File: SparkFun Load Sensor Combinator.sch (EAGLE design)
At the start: 12 parts

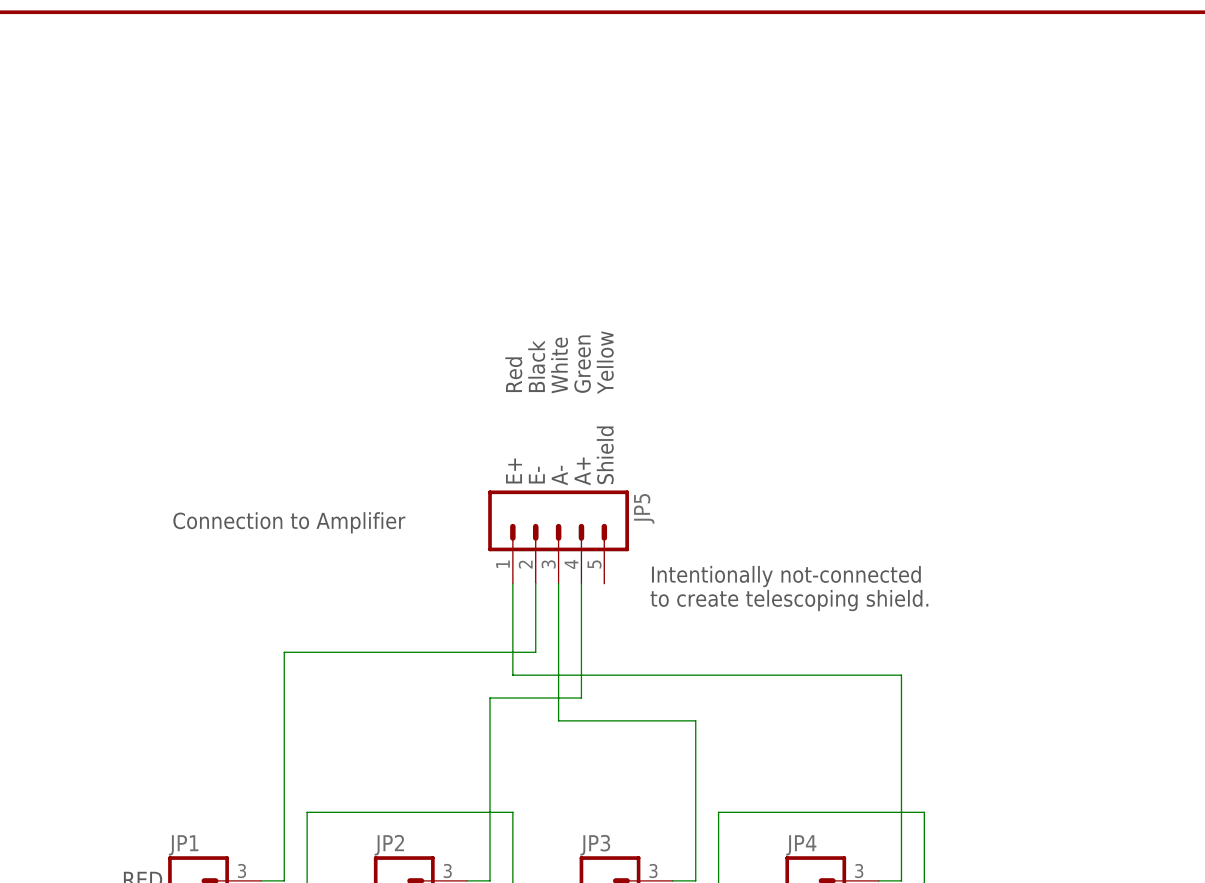
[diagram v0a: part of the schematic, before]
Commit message: Added RJ45
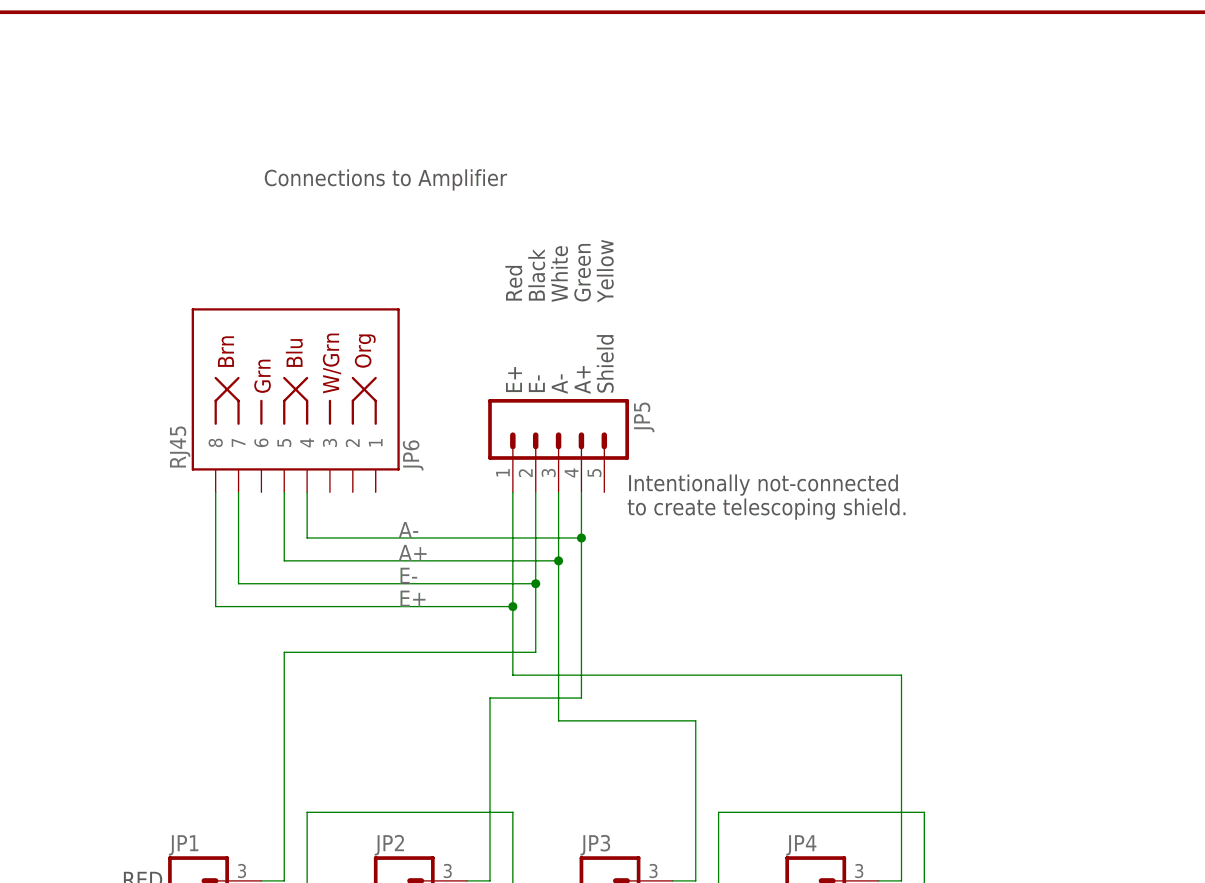
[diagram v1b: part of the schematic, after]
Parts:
- added JP6: RJ45, SparkFun-Connectors:RJ45-8PTH
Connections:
- net A+: now also JP6.5
- net A-: now also JP6.4
- net E+: now also JP6.8
- net E-: now also JP6.7
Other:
- note added: "Connections to Amplifier"
- note removed: "Connection to Amplifier"
- moved on the sheet: JP5
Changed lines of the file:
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@@
 <?xml version="1.0" encoding="utf-8"?>
 <!DOCTYPE eagle SYSTEM "eagle.dtd">
-<eagle version="7.2.0">
+<eagle version="7.1.0">
 <drawing>
 <settings>
@@
 </part>
 <part name="JP5" library="SparkFun-Connectors" deviceset="M05" device="PTH"/>
+<part name="JP6" library="SparkFun-Connectors" deviceset="RJ45-8" device="PTH" value="RJ45"/>
 </parts>
 <sheets>
 <sheet>
 <plain>
-<text x="120.396" y="132.842" size="1.778" layer="97" rot="R90">E+</text>
-<text x="122.936" y="132.842" size="1.778" layer="97" rot="R90">E-</text>
-<text x="125.476" y="132.842" size="1.778" layer="97" rot="R90">A-</text>
-<text x="128.016" y="132.842" size="1.778" layer="97" rot="R90">A+</text>
-<text x="120.396" y="143.002" size="1.778" layer="97" rot="R90">Red</text>
-<text x="122.936" y="143.002" size="1.778" layer="97" rot="R90">Black</text>
-<text x="125.476" y="143.002" size="1.778" layer="97" rot="R90">White</text>
-<text x="128.016" y="143.002" size="1.778" layer="97" rot="R90">Green</text>
+<text x="120.396" y="143.002" size="1.778" layer="97" rot="R90">E+</text>
+<text x="122.936" y="143.002" size="1.778" layer="97" rot="R90">E-</text>
+<text x="125.476" y="143.002" size="1.778" layer="97" rot="R90">A-</text>
+<text x="128.016" y="143.002" size="1.778" layer="97" rot="R90">A+</text>
+<text x="120.396" y="153.162" size="1.778" layer="97" rot="R90">Red</text>
+<text x="122.936" y="153.162" size="1.778" layer="97" rot="R90">Black</text>
+<text x="125.476" y="153.162" size="1.778" layer="97" rot="R90">White</text>
+<text x="128.016" y="153.162" size="1.778" layer="97" rot="R90">Green</text>
 <text x="147.32" y="68.58" size="1.778" layer="97">Lower Right</text>
 <text x="101.6" y="68.58" size="1.778" layer="97">Upper Right</text>
@@
 <text x="106.68" y="60.96" size="1.778" layer="97">3-Wire Load Sensors</text>
 <text x="105.41" y="63.754" size="1.778" layer="97">Common Bathroom Scale</text>
-<text x="81.534" y="128.016" size="1.778" layer="97">Connection to Amplifier</text>
+<text x="91.694" y="166.116" size="1.778" layer="97">Connections to Amplifier</text>
 <text x="75.692" y="82.804" size="1.778" layer="97">BLK</text>
 <text x="75.946" y="85.598" size="1.778" layer="97">WHT</text>
 <text x="75.946" y="88.138" size="1.778" layer="97">RED</text>
 <text x="83.82" y="53.34" size="2.032" layer="97">4 load sensors combine to create one load cell</text>
-<text x="130.556" y="132.842" size="1.778" layer="97" rot="R90">Shield</text>
-<text x="130.556" y="143.002" size="1.778" layer="97" rot="R90">Yellow</text>
-<text x="134.62" y="119.38" size="1.778" layer="97">Intentionally not-connected
+<text x="130.556" y="143.002" size="1.778" layer="97" rot="R90">Shield</text>
+<text x="130.556" y="153.162" size="1.778" layer="97" rot="R90">Yellow</text>
+<text x="132.08" y="129.54" size="1.778" layer="97">Intentionally not-connected
 to create telescoping shield.</text>
 </plain>
@@
 </instance>
 <instance part="FRAME1" gate="V" x="147.32" y="0"/>
-<instance part="JP5" gate="G$1" x="124.46" y="129.54" rot="R270"/>
+<instance part="JP5" gate="G$1" x="124.46" y="139.7" rot="R270"/>
+<instance part="JP6" gate="JP1" x="96.52" y="139.7" rot="MR90"/>
 </instances>
 <busses>
@@
 <wire x1="162.56" y1="88.9" x2="162.56" y2="111.76" width="0.1524" layer="91"/>
 <wire x1="119.38" y1="111.76" x2="162.56" y2="111.76" width="0.1524" layer="91"/>
-<wire x1="119.38" y1="111.76" x2="119.38" y2="121.92" width="0.1524" layer="91"/>
+<wire x1="119.38" y1="111.76" x2="119.38" y2="119.38" width="0.1524" layer="91"/>
 <pinref part="JP5" gate="G$1" pin="1"/>
+<wire x1="119.38" y1="119.38" x2="119.38" y2="132.08" width="0.1524" layer="91"/>
+<wire x1="119.38" y1="119.38" x2="86.36" y2="119.38" width="0.1524" layer="91"/>
+<wire x1="86.36" y1="119.38" x2="86.36" y2="132.08" width="0.1524" layer="91"/>
+<junction x="119.38" y="119.38"/>
+<pinref part="JP6" gate="JP1" pin="8"/>
+<label x="106.68" y="119.38" size="1.778" layer="95"/>
 </segment>
 </net>
@@
 <pinref part="JP3" gate="G$1" pin="3"/>
 <wire x1="139.7" y1="88.9" x2="137.16" y2="88.9" width="0.1524" layer="91"/>
-<wire x1="124.46" y1="106.68" x2="124.46" y2="121.92" width="0.1524" layer="91"/>
+<wire x1="124.46" y1="106.68" x2="124.46" y2="124.46" width="0.1524" layer="91"/>
 <pinref part="JP5" gate="G$1" pin="3"/>
+<wire x1="124.46" y1="124.46" x2="124.46" y2="132.08" width="0.1524" layer="91"/>
+<wire x1="124.46" y1="124.46" x2="93.98" y2="124.46" width="0.1524" layer="91"/>
+<junction x="124.46" y="124.46"/>
+<pinref part="JP6" gate="JP1" pin="5"/>
+<wire x1="93.98" y1="132.08" x2="93.98" y2="124.46" width="0.1524" layer="91"/>
+<label x="106.68" y="124.46" size="1.778" layer="95"/>
 </segment>
 </net>
@@
 <wire x1="116.84" y1="88.9" x2="116.84" y2="109.22" width="0.1524" layer="91"/>
 <wire x1="116.84" y1="109.22" x2="127" y2="109.22" width="0.1524" layer="91"/>
-<wire x1="127" y1="121.92" x2="127" y2="109.22" width="0.1524" layer="91"/>
+<wire x1="127" y1="132.08" x2="127" y2="127" width="0.1524" layer="91"/>
 <pinref part="JP5" gate="G$1" pin="4"/>
+<wire x1="127" y1="127" x2="127" y2="109.22" width="0.1524" layer="91"/>
+<wire x1="127" y1="127" x2="96.52" y2="127" width="0.1524" layer="91"/>
+<junction x="127" y="127"/>
+<pinref part="JP6" gate="JP1" pin="4"/>
+<wire x1="96.52" y1="132.08" x2="96.52" y2="127" width="0.1524" layer="91"/>
+<label x="106.68" y="127" size="1.778" layer="95"/>
 </segment>
 </net>
@@
 <segment>
 <wire x1="121.92" y1="114.3" x2="121.92" y2="121.92" width="0.1524" layer="91"/>
+<wire x1="121.92" y1="121.92" x2="121.92" y2="132.08" width="0.1524" layer="91"/>
 <wire x1="121.92" y1="114.3" x2="93.98" y2="114.3" width="0.1524" layer="91"/>
 <wire x1="93.98" y1="114.3" x2="93.98" y2="88.9" width="0.1524" layer="91"/>
@@
 <wire x1="93.98" y1="88.9" x2="91.44" y2="88.9" width="0.1524" layer="91"/>
 <pinref part="JP5" gate="G$1" pin="2"/>
-</segment>
-</net>
+<wire x1="121.92" y1="121.92" x2="88.9" y2="121.92" width="0.1524" layer="91"/>
+<wire x1="88.9" y1="121.92" x2="88.9" y2="132.08" width="0.1524" layer="91"/>
+<junction x="121.92" y="121.92"/>
+<pinref part="JP6" gate="JP1" pin="7"/>
+<label x="106.68" y="121.92" size="1.778" layer="95"/>
+</segment>
+</net>

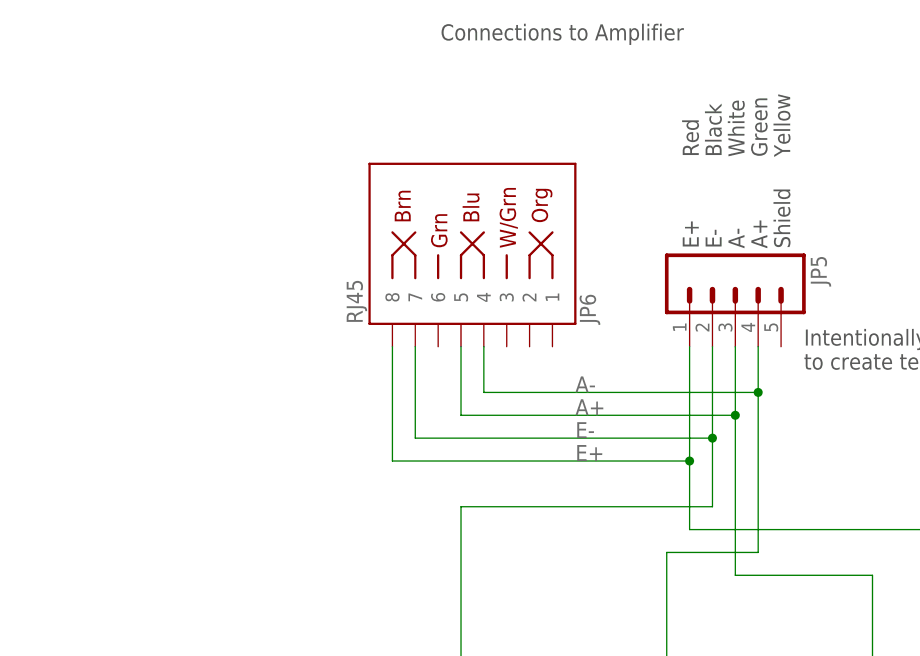
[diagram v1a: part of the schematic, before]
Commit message: Added DS18S20 connection.
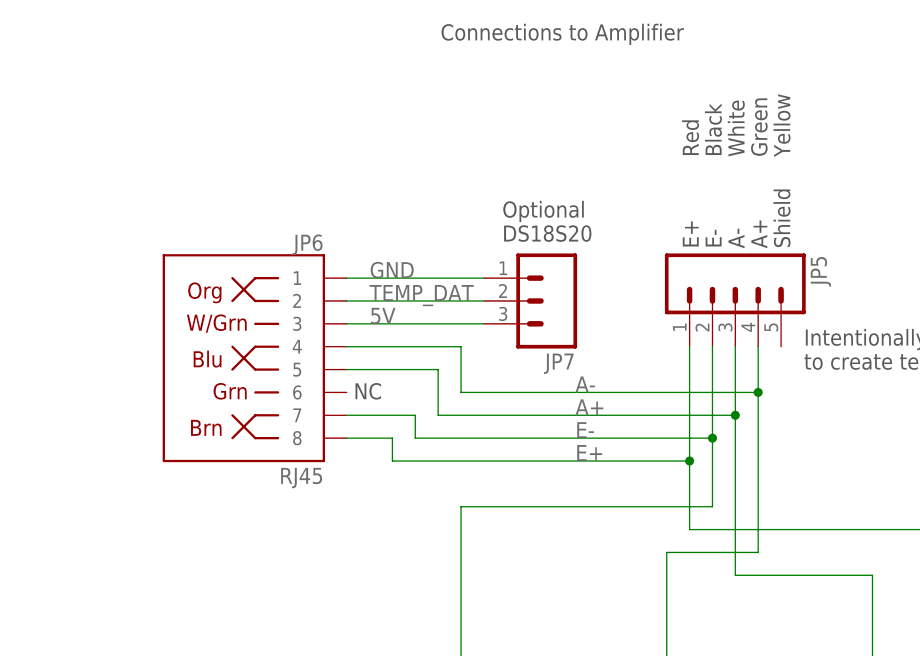
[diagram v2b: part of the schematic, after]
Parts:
- added JP7: (no value), SparkFun-Connectors:M03PTH
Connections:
- new net 5V: JP6.3, JP7.3
- new net GND: JP6.1, JP7.1
- new net TEMP_DAT: JP6.2, JP7.2
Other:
- note added: "NC"
- note added: "Optional DS18S20"
- moved on the sheet: JP6
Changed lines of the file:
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@@
 <part name="JP5" library="SparkFun-Connectors" deviceset="M05" device="PTH"/>
 <part name="JP6" library="SparkFun-Connectors" deviceset="RJ45-8" device="PTH" value="RJ45"/>
+<part name="JP7" library="SparkFun-Connectors" deviceset="M03" device="PTH"/>
 </parts>
 <sheets>
@@
 <text x="132.08" y="129.54" size="1.778" layer="97">Intentionally not-connected
 to create telescoping shield.</text>
+<text x="82.042" y="126.238" size="1.778" layer="97">NC</text>
+<text x="98.552" y="143.764" size="1.778" layer="97">Optional
+DS18S20</text>
 </plain>
 <instances>
@@
 <instance part="FRAME1" gate="V" x="147.32" y="0"/>
 <instance part="JP5" gate="G$1" x="124.46" y="139.7" rot="R270"/>
-<instance part="JP6" gate="JP1" x="96.52" y="139.7" rot="MR90"/>
+<instance part="JP6" gate="JP1" x="73.66" y="132.08" rot="MR0"/>
+<instance part="JP7" gate="G$1" x="104.14" y="137.16" rot="R180"/>
 </instances>
 <busses>
@@
 <pinref part="JP5" gate="G$1" pin="1"/>
 <wire x1="119.38" y1="119.38" x2="119.38" y2="132.08" width="0.1524" layer="91"/>
-<wire x1="119.38" y1="119.38" x2="86.36" y2="119.38" width="0.1524" layer="91"/>
-<wire x1="86.36" y1="119.38" x2="86.36" y2="132.08" width="0.1524" layer="91"/>
 <junction x="119.38" y="119.38"/>
 <pinref part="JP6" gate="JP1" pin="8"/>
 <label x="106.68" y="119.38" size="1.778" layer="95"/>
+<wire x1="119.38" y1="119.38" x2="86.36" y2="119.38" width="0.1524" layer="91"/>
+<wire x1="86.36" y1="119.38" x2="86.36" y2="121.92" width="0.1524" layer="91"/>
+<wire x1="86.36" y1="121.92" x2="81.28" y2="121.92" width="0.1524" layer="91"/>
 </segment>
 </net>
@@
 <pinref part="JP5" gate="G$1" pin="3"/>
 <wire x1="124.46" y1="124.46" x2="124.46" y2="132.08" width="0.1524" layer="91"/>
-<wire x1="124.46" y1="124.46" x2="93.98" y2="124.46" width="0.1524" layer="91"/>
+<wire x1="124.46" y1="124.46" x2="91.44" y2="124.46" width="0.1524" layer="91"/>
 <junction x="124.46" y="124.46"/>
 <pinref part="JP6" gate="JP1" pin="5"/>
-<wire x1="93.98" y1="132.08" x2="93.98" y2="124.46" width="0.1524" layer="91"/>
 <label x="106.68" y="124.46" size="1.778" layer="95"/>
+<wire x1="81.28" y1="129.54" x2="91.44" y2="129.54" width="0.1524" layer="91"/>
+<wire x1="91.44" y1="129.54" x2="91.44" y2="124.46" width="0.1524" layer="91"/>
 </segment>
 </net>
@@
 <pinref part="JP5" gate="G$1" pin="4"/>
 <wire x1="127" y1="127" x2="127" y2="109.22" width="0.1524" layer="91"/>
-<wire x1="127" y1="127" x2="96.52" y2="127" width="0.1524" layer="91"/>
+<wire x1="127" y1="127" x2="93.98" y2="127" width="0.1524" layer="91"/>
 <junction x="127" y="127"/>
 <pinref part="JP6" gate="JP1" pin="4"/>
-<wire x1="96.52" y1="132.08" x2="96.52" y2="127" width="0.1524" layer="91"/>
 <label x="106.68" y="127" size="1.778" layer="95"/>
+<wire x1="81.28" y1="132.08" x2="93.98" y2="132.08" width="0.1524" layer="91"/>
+<wire x1="93.98" y1="132.08" x2="93.98" y2="127" width="0.1524" layer="91"/>
 </segment>
 </net>
@@
 <wire x1="93.98" y1="88.9" x2="91.44" y2="88.9" width="0.1524" layer="91"/>
 <pinref part="JP5" gate="G$1" pin="2"/>
-<wire x1="121.92" y1="121.92" x2="88.9" y2="121.92" width="0.1524" layer="91"/>
-<wire x1="88.9" y1="121.92" x2="88.9" y2="132.08" width="0.1524" layer="91"/>
 <junction x="121.92" y="121.92"/>
 <pinref part="JP6" gate="JP1" pin="7"/>
 <label x="106.68" y="121.92" size="1.778" layer="95"/>
+<wire x1="121.92" y1="121.92" x2="88.9" y2="121.92" width="0.1524" layer="91"/>
+<wire x1="88.9" y1="121.92" x2="88.9" y2="124.46" width="0.1524" layer="91"/>
+<wire x1="88.9" y1="124.46" x2="81.28" y2="124.46" width="0.1524" layer="91"/>
 </segment>
 </net>
+<net name="5V" class="0">
+<segment>
+<pinref part="JP6" gate="JP1" pin="3"/>
+<pinref part="JP7" gate="G$1" pin="3"/>
+<wire x1="81.28" y1="134.62" x2="96.52" y2="134.62" width="0.1524" layer="91"/>
+<label x="83.82" y="134.62" size="1.778" layer="95"/>
+</segment>
+</net>
+<net name="TEMP_DAT" class="0">
+<segment>
+<pinref part="JP6" gate="JP1" pin="2"/>
+<pinref part="JP7" gate="G$1" pin="2"/>
+<wire x1="81.28" y1="137.16" x2="96.52" y2="137.16" width="0.1524" layer="91"/>
+<label x="83.82" y="137.16" size="1.778" layer="95"/>
+</segment>
+</net>
+<net name="GND" class="0">
+<segment>
+<pinref part="JP6" gate="JP1" pin="1"/>
+<pinref part="JP7" gate="G$1" pin="1"/>
+<wire x1="81.28" y1="139.7" x2="96.52" y2="139.7" width="0.1524" layer="91"/>
+<label x="83.82" y="139.7" size="1.778" layer="95"/>
+</segment>
+</net>

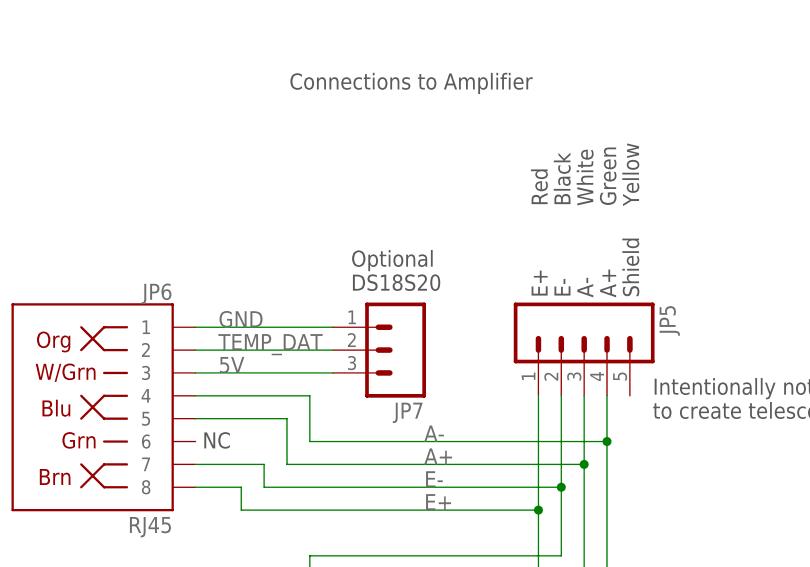
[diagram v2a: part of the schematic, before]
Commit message: Correcting name to DS18B20
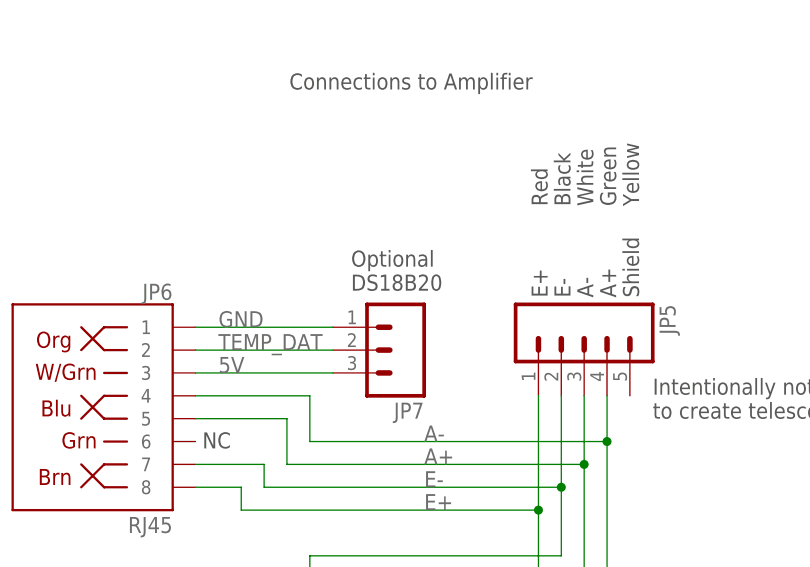
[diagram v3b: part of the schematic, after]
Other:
- note added: "Optional DS18B20"
- note removed: "Optional DS18S20"
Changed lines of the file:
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@@
 <text x="82.042" y="126.238" size="1.778" layer="97">NC</text>
 <text x="98.552" y="143.764" size="1.778" layer="97">Optional
-DS18S20</text>
+DS18B20</text>
 </plain>
 <instances>

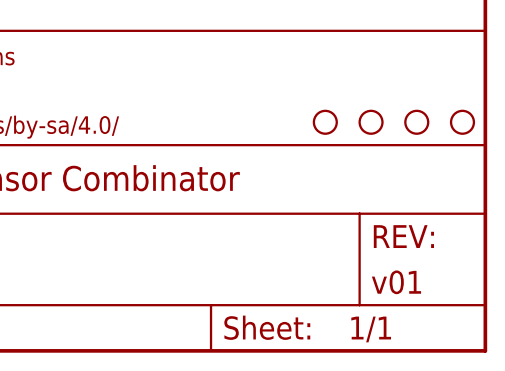
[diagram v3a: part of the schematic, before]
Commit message: Bumped silk and rev 02
Fixed issue #1
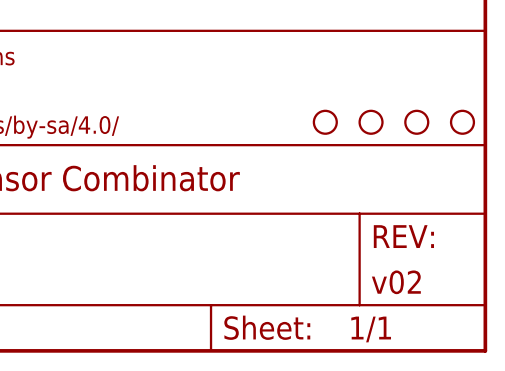
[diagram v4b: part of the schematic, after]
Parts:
- FRAME1: VERSION (none) -> v02
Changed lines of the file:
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@@
 <?xml version="1.0" encoding="utf-8"?>
 <!DOCTYPE eagle SYSTEM "eagle.dtd">
-<eagle version="7.1.0">
+<eagle version="7.2.0">
 <drawing>
 <settings>
@@
 <part name="FRAME1" library="SparkFun-Aesthetics" deviceset="FRAME-LETTER" device="">
 <attribute name="DESIGNER" value="N. Seidle"/>
+<attribute name="VERSION" value="v02"/>
 </part>
 <part name="JP5" library="SparkFun-Connectors" deviceset="M05" device="PTH"/>
